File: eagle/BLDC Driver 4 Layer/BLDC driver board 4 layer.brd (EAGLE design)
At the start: 82.5 x 67.3 mm, 45 parts, among them J2 J10MM, J3 J10MM, Q1 FDB86135, Q2 FDB86135, Q3 FDB86135, Q4 FDB86135, Q5 FDB86135, Q6 FDB86135

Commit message: Added BLDC 4 Layer Board For CAN node v3
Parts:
- removed J2, J3: J10MM, jumper:10
- added Q10, Q11, Q12, Q7, Q8, Q9: CSD173XXQX-NEXFET, ASL:CSD173XXQX
- Q1, Q2, Q3, Q4, Q5, Q6: value FDB86135 -> CSD173XXQX-NEXFET; device ASL:D2PACK -> ASL:CSD173XXQX
- moved Q6 32.5 mm to (40.6, 38.1)
- moved Q4 23.3 mm to (25.4, 27.9), turned to 180 degrees
- moved Q5 18.9 mm to (40.6, 43.2), turned to 180 degrees
- moved Q3 18.2 mm to (25.4, 33.0), turned to 180 degrees
- moved Q2 17.8 mm to (25.4, 38.1), turned to 180 degrees
- moved Q1 6.35 mm to (25.4, 43.2), turned to 180 degrees
- moved R7 2.54 mm to (30.5, 8.89)
- moved R3 2.54 mm to (14.0, 17.8)
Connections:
- removed net N$2: J2.2, Q2.1
- removed net N$5: J3.2, Q4.1
- net GH_A: now also Q11.G, Q12.G; no longer Q1.1
- net GH_B: now also Q1.G, Q2.G; no longer Q3.1
- net GH_C: now also Q3.G, Q4.G; no longer Q5.1
- net GL_A: now also Q10.G, Q9.G; no longer J2.1
- net GL_B: now also Q7.G, Q8.G; no longer J3.1
- net GL_C: now also Q5.G, Q6.G; no longer Q6.1
- net OUTPUTA: now also Q10.D, Q11.S1, Q11.S2, Q11.S3, Q12.S1, Q12.S2, Q12.S3, Q9.D; no longer Q1.3, Q2.2, Q2.P$1, Q2.P$10, Q2.P$11, Q2.P$12, Q2.P$2, Q2.P$3, Q2.P$4, Q2.P$5, Q2.P$6, Q2.P$7, Q2.P$8, Q2.P$9
- net OUTPUTB: now also Q1.S1, Q1.S2, Q1.S3, Q2.S1, Q2.S2, Q2.S3, Q7.D, Q8.D; no longer Q3.3, Q4.2, Q4.P$1, Q4.P$10, Q4.P$11, Q4.P$12, Q4.P$2, Q4.P$3, Q4.P$4, Q4.P$5, Q4.P$6, Q4.P$7, Q4.P$8, Q4.P$9
- net OUTPUTC: now also Q3.S1, Q3.S2, Q3.S3, Q4.S1, Q4.S2, Q4.S3, Q5.D, Q6.D; no longer Q5.3, Q6.2, Q6.P$1, Q6.P$10, Q6.P$11, Q6.P$12, Q6.P$2, Q6.P$3, Q6.P$4, Q6.P$5, Q6.P$6, Q6.P$7, Q6.P$8, Q6.P$9
- net SN1: now also Q7.S1, Q7.S2, Q7.S3, Q8.S1, Q8.S2, Q8.S3; no longer Q4.3
- net SN2: now also Q10.S1, Q10.S2, Q10.S3, Q9.S1, Q9.S2, Q9.S3; no longer Q2.3
- net VNEG: now also Q5.S1, Q5.S2, Q5.S3, Q6.S1, Q6.S2, Q6.S3; no longer Q6.3
- net V_BATT: now also Q1.D, Q11.D, Q12.D, Q2.D, Q3.D, Q4.D; no longer Q1.2, Q1.P$1, Q1.P$10, Q1.P$11, Q1.P$12, Q1.P$2, Q1.P$3, Q1.P$4, Q1.P$5, Q1.P$6, Q1.P$7, Q1.P$8, Q1.P$9, Q3.2, Q3.P$1, Q3.P$10, Q3.P$11, Q3.P$12, Q3.P$2, Q3.P$3, Q3.P$4, Q3.P$5, Q3.P$6, Q3.P$7, Q3.P$8, Q3.P$9, Q5.2, Q5.P$1, Q5.P$10, Q5.P$11, Q5.P$12, Q5.P$2, Q5.P$3, Q5.P$4, Q5.P$5, Q5.P$6, Q5.P$7, Q5.P$8, Q5.P$9
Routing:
- net GND: track 265.4 -> 0.00 mm, vias 7 -> 0
- net GH_B: track 222.1 -> 0.00 mm, vias 2 -> 0
- net OUTPUTC: track 130.0 -> 0.00 mm, vias 5 -> 0
- net V_BATT: track 126.0 -> 0.00 mm, vias 1 -> 0
- net SN1: track 119.4 -> 0.00 mm, vias 5 -> 0
- net OUTPUTA: track 106.2 -> 0.00 mm, vias 2 -> 0
- net CRRNTSNS2: track 98.2 -> 0.00 mm, vias 1 -> 0
- net OUTPUTB: track 97.9 -> 0.00 mm, vias 2 -> 0
- net GL_C: track 95.7 -> 0.00 mm, vias 2 -> 0
- net GH_C: track 86.0 -> 0.00 mm, vias 2 -> 0
- net SN2: track 84.5 -> 0.00 mm, vias 2 -> 0
- net PWM3: track 78.9 -> 0.00 mm
- net 3V3: track 76.9 -> 0.00 mm, vias 5 -> 0
- net VNEG: track 76.1 -> 0.00 mm, vias 13 -> 0
- net CRRNTSNS1: track 72.0 -> 0.00 mm, vias 5 -> 0
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- removed copper zone on layer 1, net GND
- removed copper zone on layer 16, net GND
- removed copper zone on layer 16, net OUTPUTA
- removed copper zone on layer 16, net OUTPUTB
- removed copper zone on layer 16, net OUTPUTC
- removed copper zone on layer 1, net VNEG
- removed copper zone on layer 16, net VNEG
- removed copper zone on layer 1, net V_BATT
- removed copper zone on layer 16, net V_BATT

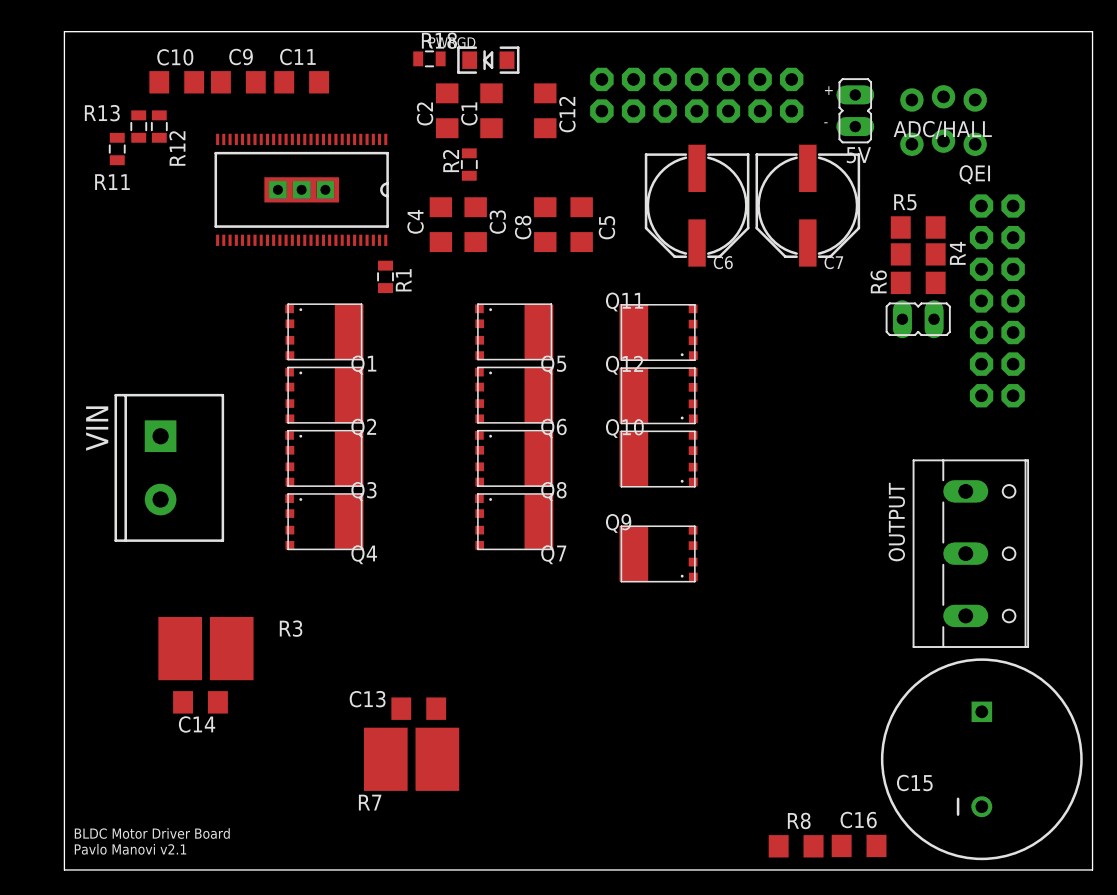
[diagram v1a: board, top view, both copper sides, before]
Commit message: More changes to the 4-Layer BLDC Board.
Signed-off-by: Pavlo Manovi <pavlo.manovi@gmail.com>
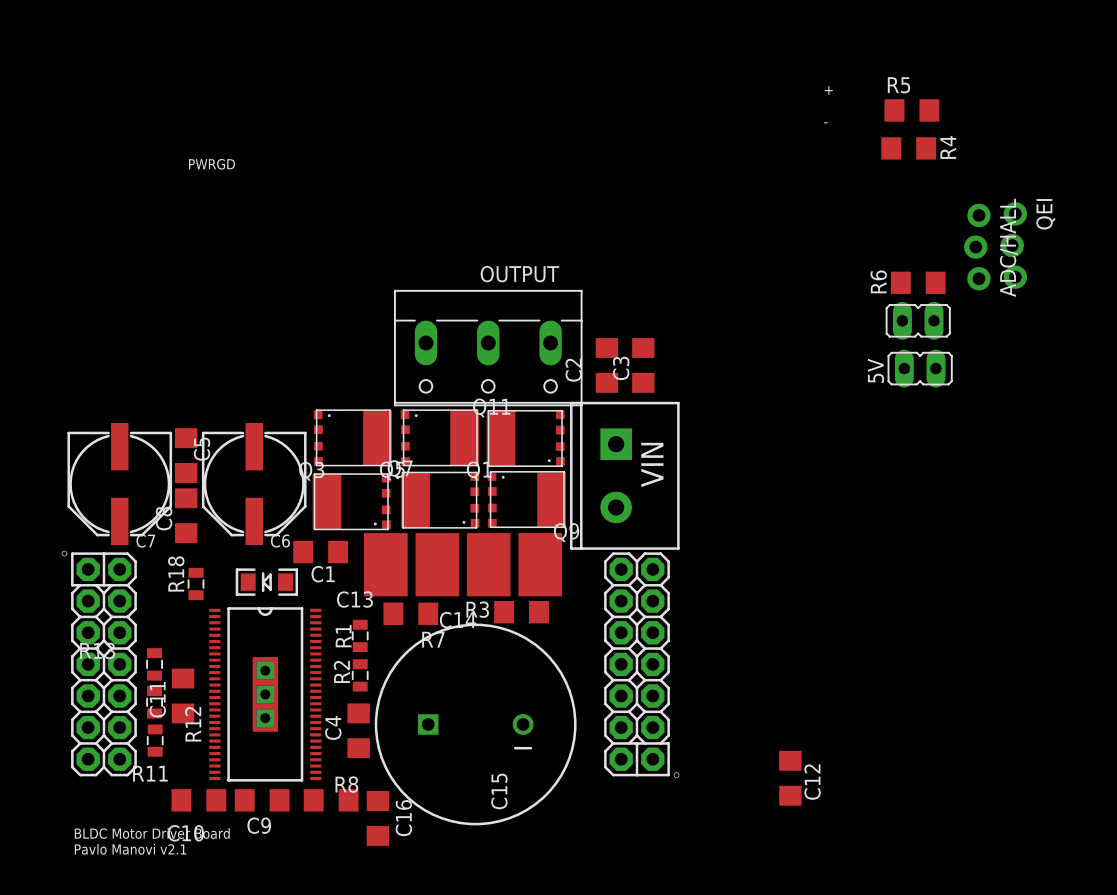
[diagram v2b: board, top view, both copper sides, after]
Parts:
- removed Q10, Q12, Q2, Q4, Q6, Q8: CSD173XXQX-NEXFET, ASL:CSD173XXQX
- U$1: value CAN_NODE_SHIELD -> CAN_NODE_SHIELD_V3; device ASL:CAN_NODE_SHIELD -> ASL:CAN_NODE_SHIELD_V3
- moved C7 59.6 mm to (6.99, 31.0)
- moved C9 57.7 mm to (18.4, 5.59), turned to 0 degrees
- moved C10 57.7 mm to (13.3, 5.59), turned to 180 degrees
- moved C12 57.1 mm to (60.8, 7.37)
- moved C11 50.2 mm to (12.1, 14.0), turned to 270 degrees
- moved R11 47.6 mm to (9.83, 10.4)
- moved R12 46.2 mm to (9.78, 13.5)
- moved R18 46.1 mm to (13.1, 23.0), turned to 90 degrees
- moved LED3 45.5 mm to (18.8, 23.1)
- moved R13 43.2 mm to (9.78, 16.5)
- moved OUTPUT 42.6 mm to (36.6, 41.0), turned to 180 degrees
- moved C6 42.0 mm to (17.8, 31.0)
- moved R2 41.9 mm to (26.3, 15.6)
- moved U$1 41.4 mm to (2.54, 0.00)
- moved C4 41.2 mm to (26.2, 11.2)
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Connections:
- net 3V3: now also U$1.CAN_HIGH, U$1.RB14; no longer U$1.P$10, U$1.P$24
- net ADC/HALL1: now also U$1.RB1; no longer U$1.P$7
- net ADC/HALL2: now also U$1.RB2; no longer U$1.P$8
- net ADC/HALL3: now also U$1.3V3; no longer U$1.P$9
- net CRRNTSNS1: now also U$1.RB8; no longer U$1.P$21
- net CRRNTSNS2: now also U$1.MCLR; no longer U$1.P$4
- net GH_A: no longer Q12.G
- net GH_B: no longer Q2.G
- net GH_C: no longer Q4.G
- net GL_A: no longer Q10.G
- net GL_B: no longer Q8.G
- net GL_C: no longer Q6.G
- net GND: now also U$1.GND1, U$1.GND3, U$1.GND5, U$1.GND7, U$1.PGD, U$1.RB12; no longer U$1.P$1, U$1.P$13, U$1.P$14, U$1.P$15, U$1.P$16, U$1.P$2, U$1.P$27, U$1.P$28
- net OUTPUTA: no longer Q10.D, Q12.S1, Q12.S2, Q12.S3
- net OUTPUTB: no longer Q2.S1, Q2.S2, Q2.S3, Q8.D
- net OUTPUTC: no longer Q4.S1, Q4.S2, Q4.S3, Q6.D
- net PWM1: now also U$1.PGC; no longer U$1.P$22
- net PWM2: now also U$1.RB9; no longer U$1.P$17
- net PWM3: now also U$1.RB15; no longer U$1.P$11
- net QEI-A: now also U$1.5V1; no longer U$1.P$19
- net QEI-B: now also U$1.RB10; no longer U$1.P$18
- net QEI-INDEX: now also U$1.GND2; no longer U$1.P$12
- net SN1: no longer Q8.S1, Q8.S2, Q8.S3
- net SN2: no longer Q10.S1, Q10.S2, Q10.S3
- net VCC: now also U$1.RA2, U$1.RB0; no longer U$1.P$20, U$1.P$6
- net VNEG: no longer Q6.S1, Q6.S2, Q6.S3
- net V_BATT: no longer Q12.D, Q2.D, Q4.D
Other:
- board outline removed

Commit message: More changes to bldc 4-layer, cleaned up files.
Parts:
- removed R4, R5, R6: 1k, CMPE118lib:1206
- added RN1: (no value), ASL:EXB-38V271JV
- moved 5V 66.8 mm to (4.45, 38.1), turned to 0 degrees
- moved ADC/HALL 64.1 mm to (13.2, 39.0), turned to 0 degrees
- moved JP3 61.7 mm to (9.68, 38.1), turned to 180 degrees
- moved QEI 54.2 mm to (26.3, 39.0), turned to 180 degrees
- moved C12 52.7 mm to (9.91, 20.8), turned to 90 degrees
- moved C3 34.7 mm to (43.6, 6.25), turned to 52.5 degrees
- moved C2 32.0 mm to (19.3, 23.0), turned to 180 degrees
- moved LED3 3.54 mm to (15.4, 24.0), turned to 270 degrees
- moved C16 3.34 mm to (27.2, 7.44), turned to 120 degrees
- moved R2 1.66 mm to (27.2, 17.0), turned to 0 degrees
- moved C4 1.21 mm to (26.4, 12.4)
- moved VIN 0.60 mm to (47.3, 31.3)
- moved R1 0.51 mm to (26.3, 19.3)
- moved C10 0.25 mm to (13.3, 5.84)
- moved C9 0.25 mm to (18.4, 5.84)
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- renumbered U$1 to U$2
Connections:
- net 3V3: now also U$2.3V3, U$2.3V31; no longer U$2.CAN_HIGH, U$2.RB14
- net ADC/HALL1: now also RN1.P$2, U$2.RB0; no longer R6.1, U$2.RB1
- net ADC/HALL2: now also RN1.P$3, U$2.RB1; no longer R5.1, U$2.RB2
- net ADC/HALL3: now also RN1.P$1, U$2.RB2; no longer R4.1, U$2.3V3
- net CRRNTSNS1: now also U$2.RA2; no longer U$2.RB8
- net CRRNTSNS2: now also U$2.A0; no longer U$2.MCLR
- net GND: now also U$2.GND, U$2.GND2, U$2.GND4, U$2.GND6; no longer U$2.PGD, U$2.RB12
- net N$13: now also RN1.P$6, RN1.P$7, RN1.P$8; no longer R4.2, R5.2, R6.2
- net PWM1: now also U$2.RB8; no longer U$2.PGC
- net PWM2: now also U$2.RB12; no longer U$2.RB9
- net PWM3: now also U$2.RB14; no longer U$2.RB15
- net QEI-A: now also U$2.RB10; no longer U$2.5V1
- net QEI-B: now also U$2.RB9; no longer U$2.RB10
- net QEI-INDEX: now also U$2.RB15; no longer U$2.GND2
- net VCC: now also U$2.5V, U$2.5V1; no longer U$2.RA2, U$2.RB0
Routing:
- net ADC/HALL2: track 0.00 -> 93.3 mm
- net 3V3: track 0.00 -> 81.3 mm, vias 0 -> 4
- net ADC/HALL1: track 0.00 -> 79.7 mm
- net GL_A: track 0.00 -> 70.1 mm, vias 0 -> 2
- net OUTPUTC: track 0.00 -> 66.2 mm
- net ADC/HALL3: track 0.00 -> 62.9 mm
- net GH_B: track 0.00 -> 58.1 mm, vias 0 -> 3
- net PWM3: track 0.00 -> 51.6 mm, vias 0 -> 1
- net OUTPUTA: track 0.00 -> 51.5 mm, vias 0 -> 1
- net QEI-B: track 0.00 -> 51.0 mm
- net QEI-A: track 0.00 -> 47.7 mm
- net CRRNTSNS2: track 0.00 -> 46.6 mm, vias 0 -> 1
- net QEI-INDEX: track 0.00 -> 44.7 mm
- net GH_A: track 0.00 -> 44.1 mm, vias 0 -> 3
- net GL_B: track 0.00 -> 39.3 mm, vias 0 -> 4
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- added copper zone on layer 1, net GND
- added copper zone on layer 16, net GND
- added copper zone on layer 2, net VNEG
- added copper zone on layer 15, net V_BATT

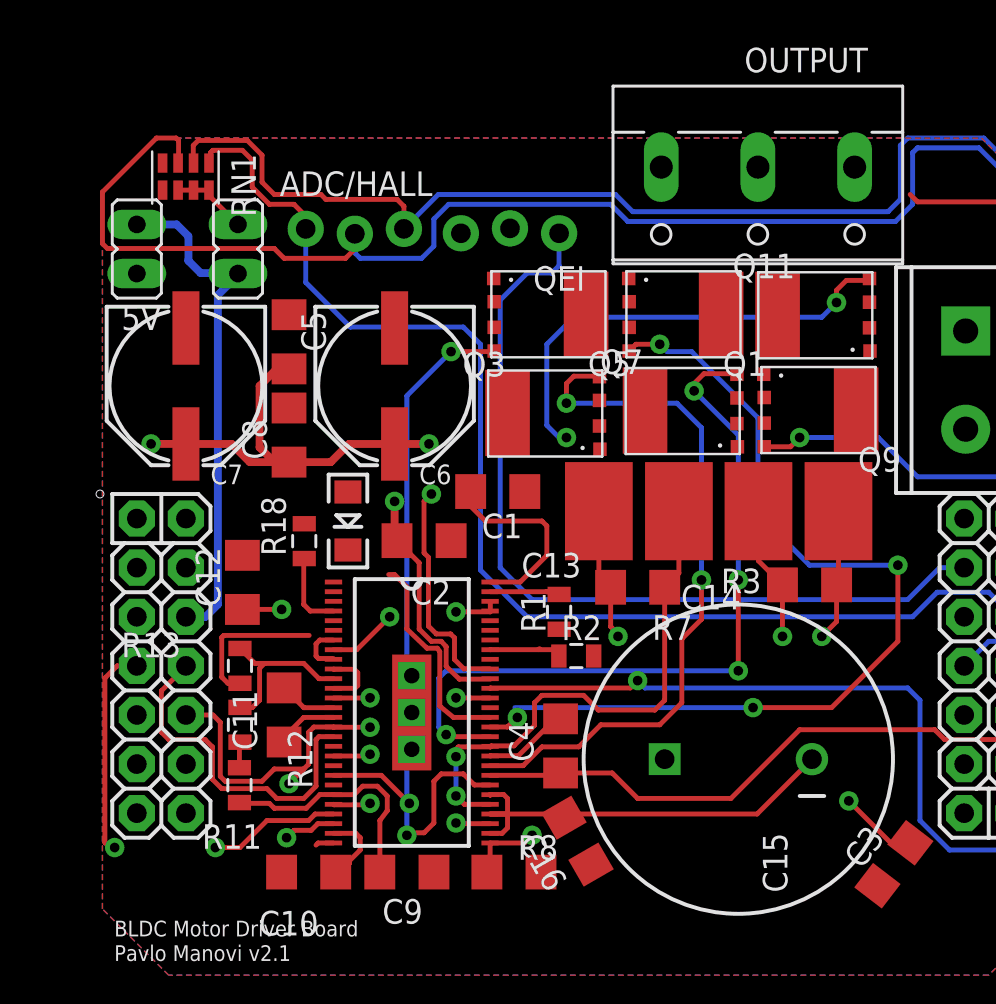
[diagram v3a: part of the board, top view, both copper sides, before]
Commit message: 4-layer bldc work, finding more space.
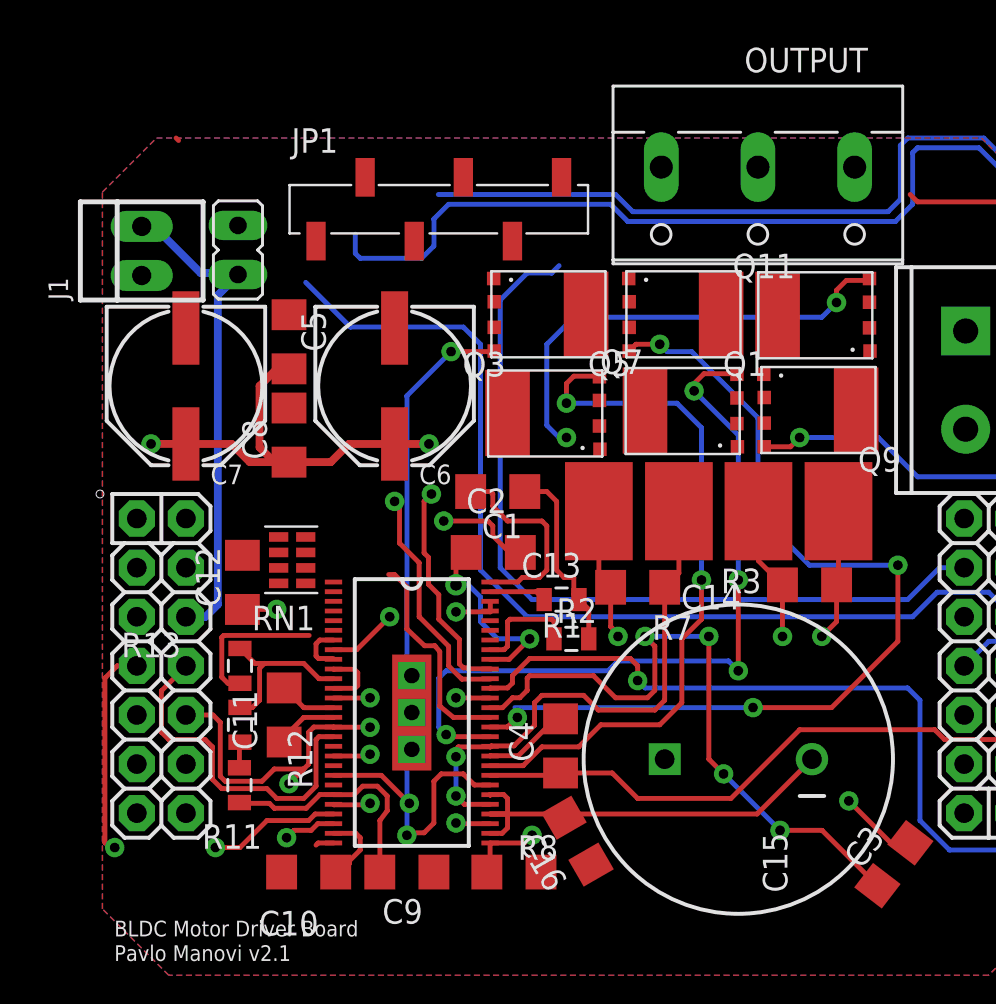
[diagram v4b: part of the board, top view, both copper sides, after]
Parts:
- removed 5V: (no value), jumper:JP1
- removed ADC/HALL, QEI: (no value), CMPE118lib:1X03_LOCK_NO_SILK
- removed LED3: (no value), ASL:LED-1206
- removed R18: 330, ASL:0805
- added J1: (no value), ASL:SOCKET-MALE-2.54MM-2
- added JP1: (no value), ASL:1X06_SMD_STRAIGHT
- moved RN1 22.3 mm to (13.2, 20.8), turned to 90 degrees
- moved C2 3.63 mm to (22.9, 22.4), turned to 0 degrees
- moved R2 0.92 mm to (26.9, 17.9)
- moved R1 0.65 mm to (26.4, 19.9), turned to 0 degrees
- moved JP3 0.05 mm to (9.68, 38.0)
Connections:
- removed net N$11: DRV8301.4, R18.1
- removed net N$15: LED3.C, R18.2
- new net N$2: DRV8301.6, U$2.PGC
- net 3V3: no longer LED3.A
- net ADC/HALL1: now also JP1.6; no longer ADC/HALL.3
- net ADC/HALL2: now also JP1.5; no longer ADC/HALL.2
- net ADC/HALL3: now also JP1.4; no longer ADC/HALL.1
- net GND: now also J1.1; no longer 5V.1
- net QEI-A: now also JP1.3; no longer QEI.3
- net QEI-B: now also JP1.2; no longer QEI.2
- net QEI-INDEX: now also JP1.1; no longer QEI.1
- net VCC: now also J1.2; no longer 5V.2
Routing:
- net N$6: track 0.00 -> 34.3 mm, vias 0 -> 4
- net ADC/HALL2: track 93.3 -> 70.1 mm
- net QEI-A: track 47.7 -> 26.4 mm
- net ADC/HALL1: track 79.7 -> 61.8 mm
- net ADC/HALL3: track 62.9 -> 51.7 mm
- net N$4: track 0.00 -> 10.1 mm, vias 0 -> 2
- net GND: track 14.5 -> 24.3 mm
- net OUTPUTA: track 51.5 -> 58.9 mm, vias 1 -> 2
- net N$11: track 4.07 -> 0.00 mm
- net N$13: track 4.00 -> 0.00 mm
- net QEI-B: track 51.0 -> 47.6 mm
- net N$3: track 3.96 -> 5.66 mm
- net QEI-INDEX: track 44.7 -> 43.0 mm
- net GL_A: track 70.1 -> 71.7 mm
- net N$1: track 10.2 -> 11.3 mm
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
